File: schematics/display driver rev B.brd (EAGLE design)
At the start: 180 x 120 mm, 78 parts, among them U1 ATF1502AS, U10 TLC5916IN, U11 TLC5916IN, U12 TLC5916IN, U13 TLC5916IN, U14 TLC5916IN, U15 TLC5916IN, U16 TLC5916IN, U17 TLC5916IN, U18 TLC5916IN, U19 TLC5916IN, U2 74LS688N, U20 TLC5916IN, U21 TLC5916IN, U22 TLC5916IN, U23 TLC5916IN, U24 TLC5916IN, U3 74HC688, U4 74HC32, U5 74HC00, U6 74HC573N, U7 74HC138, U8 TLC5916IN, U9 TLC5916IN

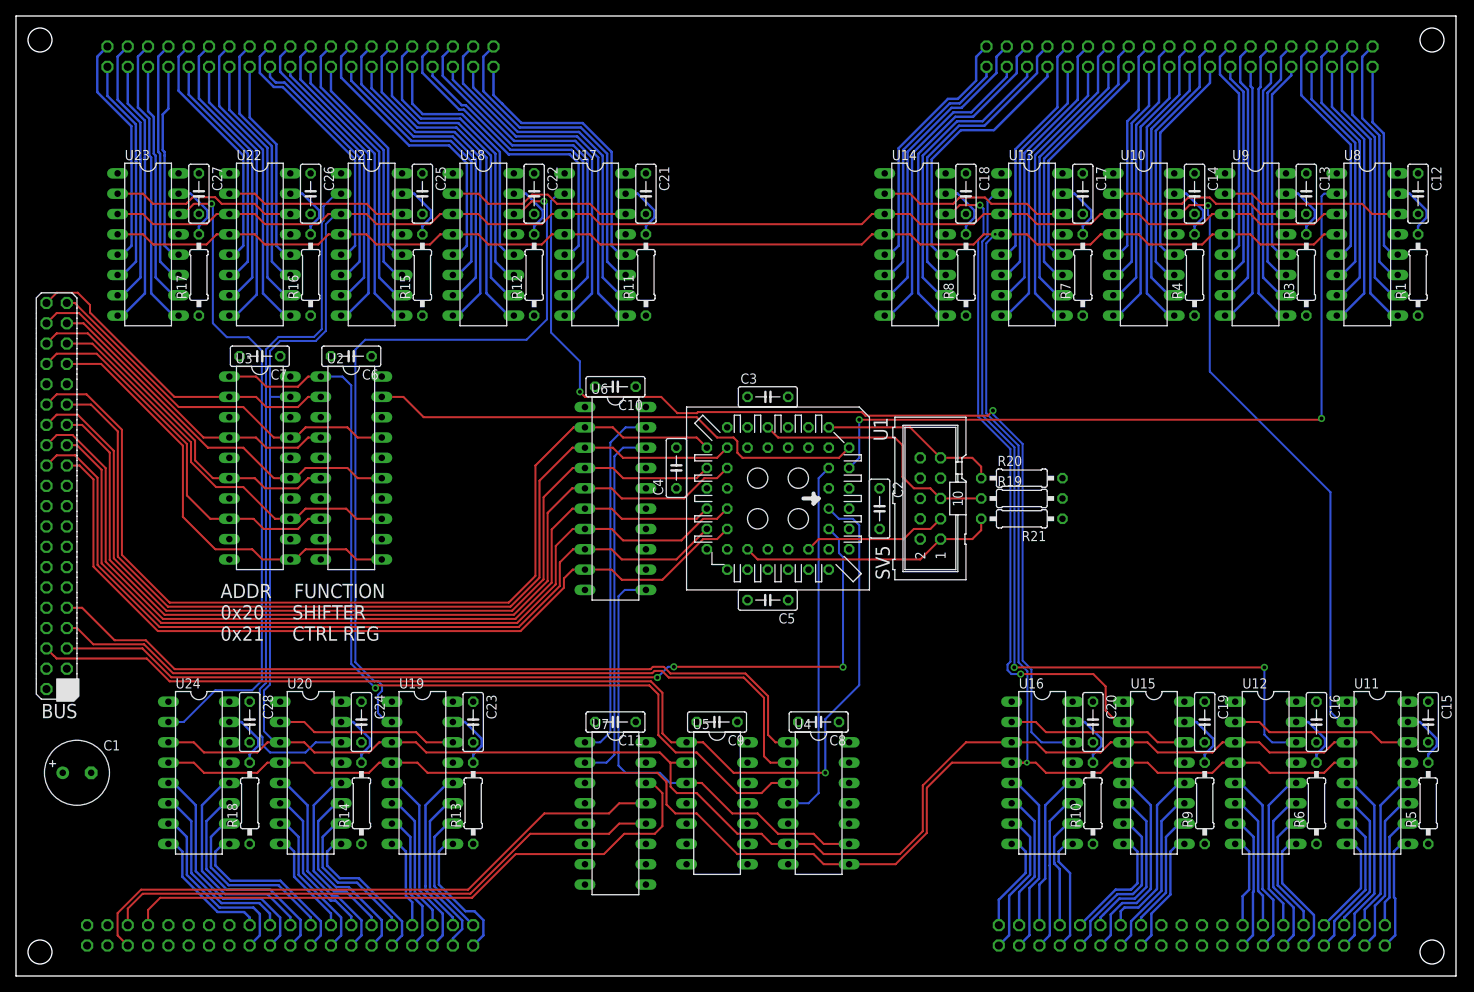
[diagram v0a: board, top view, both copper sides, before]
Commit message: Space things out a little more on the board
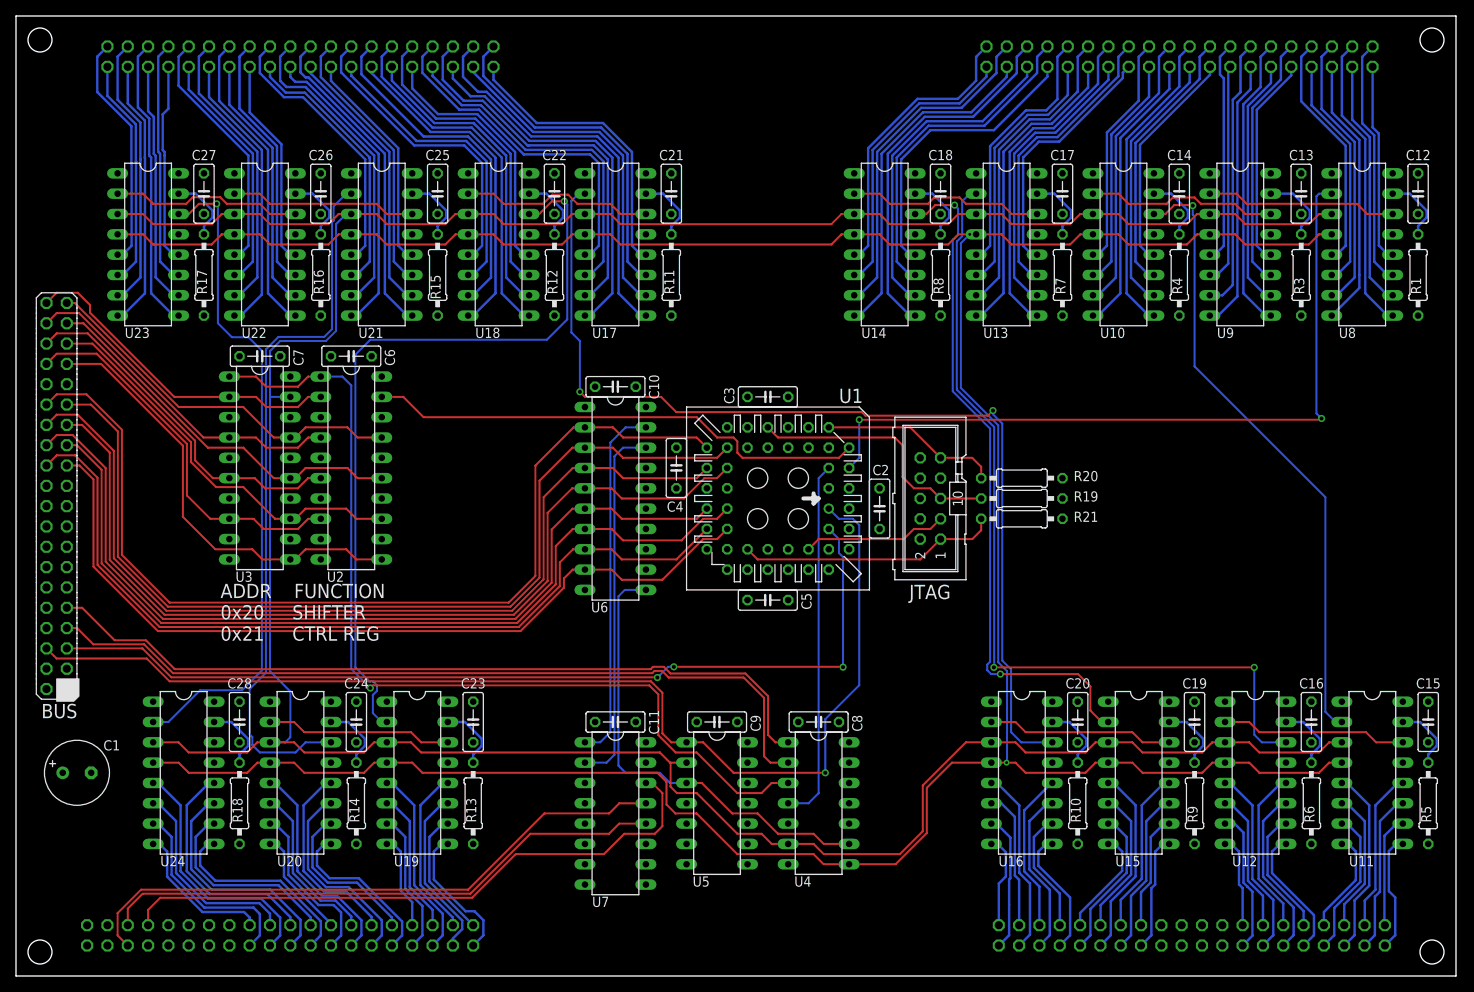
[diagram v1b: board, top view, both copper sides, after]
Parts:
- R19, R20, R21: value (none) -> 10K
- moved U14 3.81 mm to (108.6, 91.4)
- moved C18 3.18 mm to (115.6, 97.8)
- moved C21 3.18 mm to (81.9, 97.8)
- moved R11 3.18 mm to (81.9, 87.6)
- moved R8 3.18 mm to (115.6, 87.6)
- moved U13 3.17 mm to (123.8, 91.4)
- moved C22 2.54 mm to (67.3, 97.8)
- moved R12 2.54 mm to (67.3, 87.6)
- moved U16 2.54 mm to (125.7, 25.4)
- moved U17 2.54 mm to (74.9, 91.4)
- moved C17 2.54 mm to (130.8, 97.8)
- moved R7 2.54 mm to (130.8, 87.6)
- moved U10 2.54 mm to (138.4, 91.4)
- moved C14 1.91 mm to (145.4, 97.8)
- moved C20 1.91 mm to (132.7, 31.8)
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- renumbered SV5 to JTAG
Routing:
- net COL2_C: track 37.4 -> 41.2 mm
- net COL2_N: track 38.0 -> 41.8 mm
- net COL2_E: track 32.4 -> 36.2 mm
- net COL2_D: track 38.5 -> 42.3 mm
- net COL2_P: track 42.4 -> 46.2 mm
- net COL2_F: track 32.4 -> 36.2 mm
- net COL2_B: track 33.0 -> 36.8 mm
- net COL2_R: track 39.1 -> 42.9 mm
- net N$1: track 409.9 -> 413.5 mm
- net COL4_K: track 45.2 -> 48.2 mm
- net COL2_T: track 34.3 -> 37.1 mm
- net COL2_U: track 39.2 -> 42.0 mm
- net COL2_K: track 36.0 -> 38.8 mm
- net COL2_G: track 28.7 -> 31.5 mm
- net COL2_A: track 29.8 -> 32.6 mm
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
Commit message: Tidy up a little
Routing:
- net N$53: track 400.3 -> 401.4 mm, vias 2 -> 1
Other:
- board text added: "ADDR ---- 0x20 0x21"
- board text added: "FUNCTION ------- SHIFTER CONTROL REG"
- board text removed: "ADDR FUNCTION 0x20 SHIFTER 0x21 CTRL REG"
